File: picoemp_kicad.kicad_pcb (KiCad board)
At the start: 2 copper layers, 40 x 116 mm, 173 parts, among them J1 EDGE-SMA, J2 USB_C_Receptacle_USB2.0, J3 BG306-02-A-2-0400-L-G, J5 Conn_01x03_Socket, J6 Conn_01x08_Socket, P2 Header 2, P3 Header 4, Q1 LDA111STR, Q2 RGT16BM65DTL, Q3 AO3422, Q4 AO3422, Q5 FSS2301S, Q6 FSS2302S, Q7 FSS2302S, SW1 ARM, SW2 PULSE, SW3 TL3301AF160QJ, SW4 SW_SPST, SW5 SSSS811101, SW6 SSSS811101, T1 ATB322524, T2 ATB322524, U1 RP2040, U2 W25Q128JVSIQ, U3 LP4054H, U4 XB6536A, U5 ME2807, U6 LP3992-3.3, U7 LPW5206, Y1 X322512MSB4SI

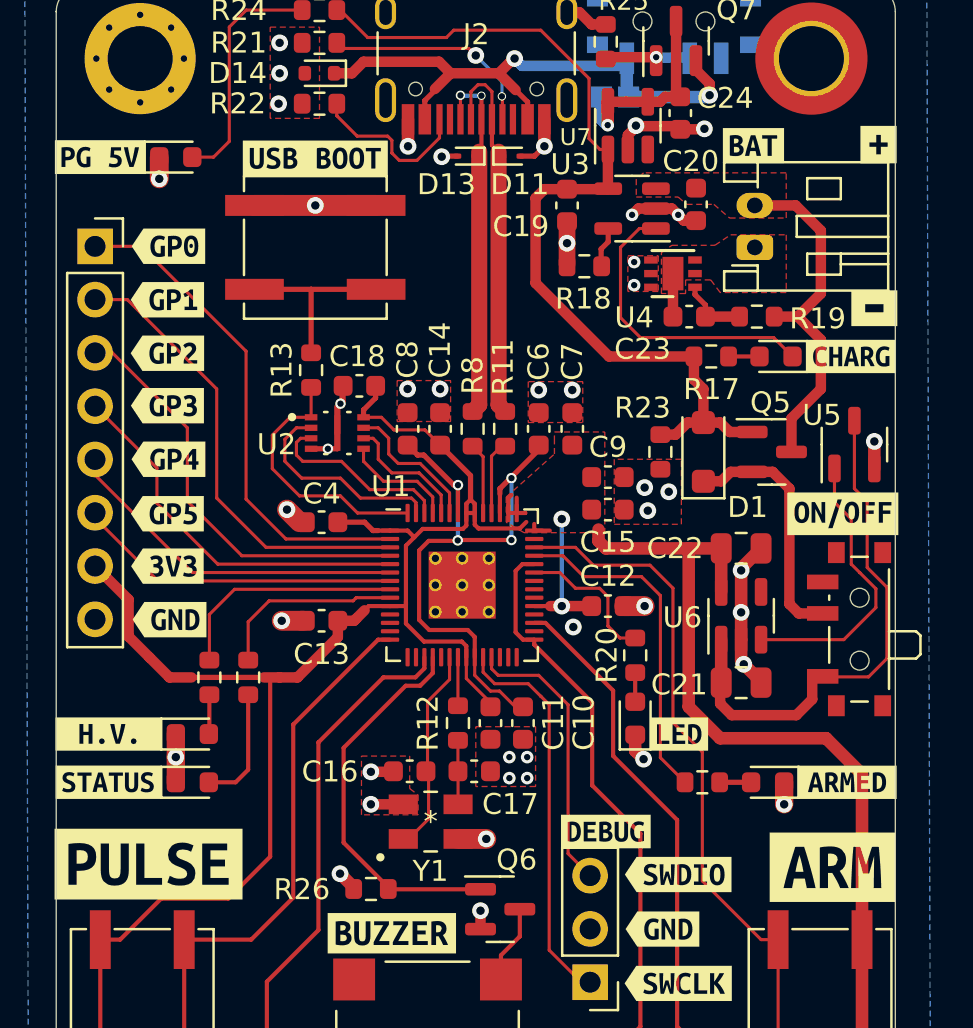
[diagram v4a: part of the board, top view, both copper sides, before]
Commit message: Minor adjustment to silkscreen
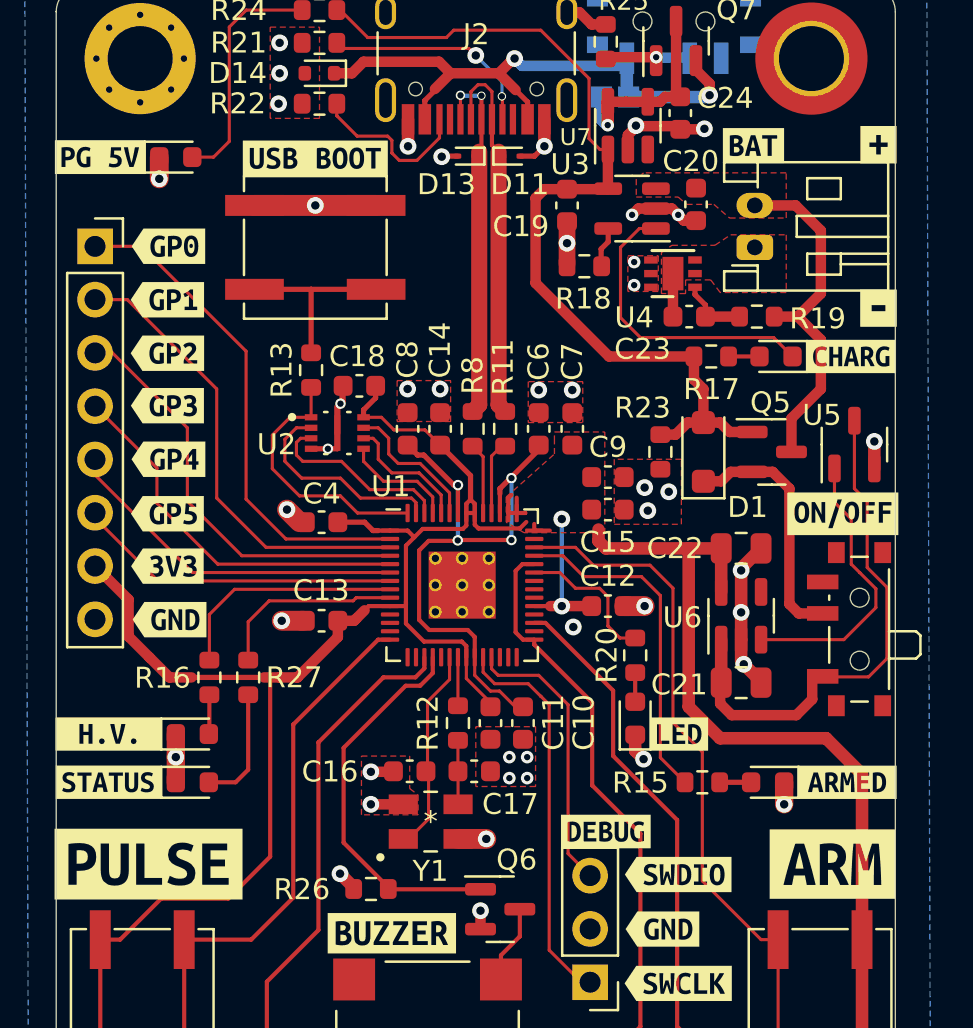
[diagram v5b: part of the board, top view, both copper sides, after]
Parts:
- removed kibuzzard-63F78DFD: G***, kibuzzard-63F78DFD
- added kibuzzard-640461F9: G***, kibuzzard-640461F9, F.Cu at (167.7, 62.4)
- moved kibuzzard-63F2726C 0.15 mm to (165.5, 88.9)
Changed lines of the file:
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@@
   )
   (footprint "kibuzzard-63F2726C" (layer "F.Cu")
-    (at 165.501105 89.0536)
+    (at 165.501105 88.9036)
     (descr "Generated with KiBuzzard")
     (tags "kb_params=eyJBbGlnbm1lbnRDaG9pY2UiOiAiQ2VudGVyIiwgIkNhcExlZnRDaG9pY2UiOiAiWyIsICJDYXBSaWdodENob2ljZSI6ICJdIiwgIkZvbnRDb21ib0JveCI6ICJVYnVudHVNb25vLUIiLCAiSGVpZ2h0Q3RybCI6ICIyIiwgIkxheWVyQ29tYm9Cb3giOiAiRi5TaWxrUyIsICJNdWx0aUxpbmVUZXh0IjogIkFSTVxuIiwgIlBhZGRpbmdCb3R0b21DdHJsIjogIjUiLCAiUGFkZGluZ0xlZnRDdHJsIjogIjUiLCAiUGFkZGluZ1JpZ2h0Q3RybCI6ICI1IiwgIlBhZGRpbmdUb3BDdHJsIjogIjUiLCAiV2lkdGhDdHJsIjogIjIifQ==")
     (attr board_only exclude_from_pos_files exclude_from_bom)
     (fp_text reference "kibuzzard-63F2726C" (at 0 -4.703233) (layer "F.SilkS") hide
-        (effects (font (size 0 0) (thickness 0.15)))
+        (effects (font (size 0.0254 0.0254) (thickness 0.00635)))
     )
     (fp_text value "G***" (at 0 4.703233) (layer "F.SilkS") hide
-        (effects (font (size 0 0) (thickness 0.15)))
+        (effects (font (size 0.0254 0.0254) (thickness 0.00635)))
     )
     (fp_poly
@@
     (property "ki_keywords" "cap capacitor")
     (attr smd)
-    (fp_text reference "C13" (at 0.001105 -1.5964) (layer "F.SilkS")
+    (fp_text reference "C13" (at 0.021105 1.4436) (layer "F.SilkS")
         (effects (font (size 1 1) (thickness 0.15)))
     )
@@
   )
   (footprint "kibuzzard-63F78E1E" (layer "F.Cu")
-    (at 167.701105 54.6036)
+    (at 167.7 54.61)
     (descr "Generated with KiBuzzard")
     (tags "kb_params=eyJBbGlnbm1lbnRDaG9pY2UiOiAiQ2VudGVyIiwgIkNhcExlZnRDaG9pY2UiOiAiWyIsICJDYXBSaWdodENob2ljZSI6ICJdIiwgIkZvbnRDb21ib0JveCI6ICJVYnVudHVNb25vLUIiLCAiSGVpZ2h0Q3RybCI6ICIxLjMiLCAiTGF5ZXJDb21ib0JveCI6ICJGLlNpbGtTIiwgIk11bHRpTGluZVRleHQiOiAiKyIsICJQYWRkaW5nQm90dG9tQ3RybCI6ICI1IiwgIlBhZGRpbmdMZWZ0Q3RybCI6ICI1IiwgIlBhZGRpbmdSaWdodEN0cmwiOiAiNSIsICJQYWRkaW5nVG9wQ3RybCI6ICI1IiwgIldpZHRoQ3RybCI6ICIxLiJ9")
@@
     (property "ki_keywords" "R res resistor")
     (attr smd)
-    (fp_text reference "R16" (at -3.35 -0.05 -270) (layer "F.SilkS") hide
+    (fp_text reference "R16" (at 0.0264 2.231105 -180) (layer "F.SilkS")
         (effects (font (size 1 1) (thickness 0.15)))
     )
@@
       (stroke (width 0) (type solid)) (fill solid) (layer "F.SilkS"))
   )
-  (footprint "kibuzzard-63F78DFD" (layer "F.Cu")
-    (at 167.501105 62.4036)
-    (descr "Generated with KiBuzzard")
-    (tags "kb_params=eyJBbGlnbm1lbnRDaG9pY2UiOiAiQ2VudGVyIiwgIkNhcExlZnRDaG9pY2UiOiAiWyIsICJDYXBSaWdodENob2ljZSI6ICJdIiwgIkZvbnRDb21ib0JveCI6ICJVYnVudHVNb25vLUIiLCAiSGVpZ2h0Q3RybCI6ICIyIiwgIkxheWVyQ29tYm9Cb3giOiAiRi5TaWxrUyIsICJNdWx0aUxpbmVUZXh0IjogIi1cbiIsICJQYWRkaW5nQm90dG9tQ3RybCI6ICI1IiwgIlBhZGRpbmdMZWZ0Q3RybCI6ICI1IiwgIlBhZGRpbmdSaWdodEN0cmwiOiAiNSIsICJQYWRkaW5nVG9wQ3RybCI6ICI1IiwgIldpZHRoQ3RybCI6ICIxLiJ9")
-    (attr board_only exclude_from_pos_files exclude_from_bom)
-    (fp_text reference "kibuzzard-63F78DFD" (at 0 -3.901546) (layer "F.SilkS") hide
-        (effects (font (size 0 0) (thickness 0.15)))
-    )
-    (fp_text value "G***" (at 0 3.901546) (layer "F.SilkS") hide
-        (effects (font (size 0 0) (thickness 0.15)))
-    )
-    (fp_poly
-      (pts
-        (xy -0.434975 -0.853546)
-        (xy -1.096433 -0.853546)
-        (xy -1.096433 0.853546)
-        (xy -0.434975 0.853546)
-        (xy 0.434975 0.853546)
-        (xy 0.434975 0.192087)
-        (xy -0.434975 0.192087)
-        (xy -0.434975 -0.192088)
-        (xy 0.434975 -0.192088)
-        (xy 0.434975 0.192087)
-        (xy 0.434975 0.853546)
-        (xy 1.096433 0.853546)
-        (xy 1.096433 -0.853546)
-        (xy 0.434975 -0.853546)
-        (xy -0.434975 -0.853546)
-      )
-      (stroke (width 0) (type solid)) (fill solid) (layer "F.SilkS"))
-  )
   (footprint "Capacitor_SMD:C_0603_1608Metric" (layer "F.Cu")
     (at 159.001105 57.4536 -90)
@@
       (stroke (width 0) (type solid)) (fill solid) (layer "F.SilkS"))
   )
+  (footprint "kibuzzard-640461F9" (layer "F.Cu")
+    (at 167.7 62.4)
+    (descr "Generated with KiBuzzard")
+    (tags "kb_params=eyJBbGlnbm1lbnRDaG9pY2UiOiAiQ2VudGVyIiwgIkNhcExlZnRDaG9pY2UiOiAiWyIsICJDYXBSaWdodENob2ljZSI6ICJdIiwgIkZvbnRDb21ib0JveCI6ICJVYnVudHVNb25vLUIiLCAiSGVpZ2h0Q3RybCI6ICIxLjUiLCAiTGF5ZXJDb21ib0JveCI6ICJGLlNpbGtTIiwgIk11bHRpTGluZVRleHQiOiAiLVxuIiwgIlBhZGRpbmdCb3R0b21DdHJsIjogIjcuNSIsICJQYWRkaW5nTGVmdEN0cmwiOiAiNS41IiwgIlBhZGRpbmdSaWdodEN0cmwiOiAiNS41IiwgIlBhZGRpbmdUb3BDdHJsIjogIjcuNSIsICJXaWR0aEN0cmwiOiAiMS4ifQ==")
+    (attr board_only exclude_from_pos_files exclude_from_bom)
+    (fp_text reference "kibuzzard-640461F9" (at 0 -3.936206) (layer "F.SilkS") hide
+        (effects (font (size 1 1) (thickness 0.25)))
+    )
+    (fp_text value "G***" (at 0 3.936206) (layer "F.SilkS") hide
+        (effects (font (size 1 1) (thickness 0.25)))
+    )
+    (fp_poly
+      (pts
+        (xy -0.326231 -0.888206)
+        (xy -0.871934 -0.888206)
+        (xy -0.871934 0.888206)
+        (xy -0.326231 0.888206)
+        (xy 0.326231 0.888206)
+        (xy 0.326231 0.144066)
+        (xy -0.326231 0.144066)
+        (xy -0.326231 -0.144066)
+        (xy 0.326231 -0.144066)
+        (xy 0.326231 0.144066)
+        (xy 0.326231 0.888206)
+        (xy 0.871934 0.888206)
+        (xy 0.871934 -0.888206)
+        (xy 0.326231 -0.888206)
+        (xy -0.326231 -0.888206)
+      )
+      (stroke (width 0) (type solid)) (fill solid) (layer "F.SilkS"))
+  )
   (footprint "Connector_PinHeader_2.54mm:PinHeader_1x03_P2.54mm_Vertical" (layer "F.Cu")
     (at 153.951105 94.5336 180)
@@
     (property "ki_keywords" "R res resistor")
     (attr smd)
-    (fp_text reference "R27" (at 0 -1.43 -270) (layer "F.SilkS") hide
+    (fp_text reference "R27" (at 0.0064 -2.188895 -180) (layer "F.SilkS")
         (effects (font (size 1 1) (thickness 0.15)))
     )
@@
     (property "ki_keywords" "R res resistor")
     (attr smd)
-    (fp_text reference "R15" (at -2.95 0.1) (layer "F.SilkS") hide
+    (fp_text reference "R15" (at -2.951105 0.0264) (layer "F.SilkS")
         (effects (font (size 1 1) (thickness 0.15)))
     )
